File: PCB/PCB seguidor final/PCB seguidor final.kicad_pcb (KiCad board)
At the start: 2 copper layers, 37 parts, among them J2 MOTOR A, J3 MOTOR B, J4 Conn_01x08, J6 Conn_01x04, SW1 SW_SPDT, U2 ESP32-DEVKIT-V1, U3 LM7805, U4 ROB-14450, U5 ROB-14450, U6 module_mpu6050

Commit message: avance
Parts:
- moved J6 209.0 mm to (264.3, 137.1)
- moved U2 202.9 mm to (228.9, 92.0)
- moved J4 186.5 mm to (266.0, 100.0), turned to 180 degrees
- moved U6 183.9 mm to (261.1, 83.3), turned to 60 degrees
- moved U7 142.4 mm to (169.5, 125.9)
- moved U1 128.0 mm to (169.0, 75.2)
- moved U4 112.4 mm to (158.0, 115.5), turned to -90 degrees
- moved U3 99.2 mm to (17.6, 124.3)
- moved U5 77.8 mm to (157.7, 68.0), turned to -90 degrees
- moved C3 67.9 mm to (29.6, 156.1)
- moved .1 54.8 mm to (83.8, 121.1)
- moved C4 37.9 mm to (44.3, 127.5)
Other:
- board outline added: 149.7 x 69.6 mm

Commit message: Acabada(esperando corrección)
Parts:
- moved S2 135.2 mm to (177.9, 127.0)
- moved S1 133.4 mm to (177.9, 115.9)
- moved S4 127.6 mm to (188.0, 122.3)
- moved GND1 127.4 mm to (202.2, 120.9), turned to 90 degrees
- moved R2 122.1 mm to (193.1, 118.3), turned to -90 degrees
- moved S3 118.4 mm to (167.5, 122.2)
- moved R4 117.1 mm to (190.7, 118.2), turned to -90 degrees
- moved C3 108.9 mm to (120.4, 96.1)
- moved R1 107.9 mm to (171.7, 118.1), turned to -90 degrees
- moved R3 103.0 mm to (169.8, 118.1), turned to -90 degrees
- moved U3 96.6 mm to (110.0, 96.2)
- moved TURBINA1 81.0 mm to (161.8, 110.0), turned to 180 degrees
- moved H3 78.4 mm to (97.9, 129.7)
- moved C2 78.2 mm to (98.7, 96.0)
- moved C1 77.7 mm to (98.8, 84.6), turned to 180 degrees
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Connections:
- GND1 pad 3: VCC -> +5V
- SW1 pad 1: unconnected-(SW1-A-Pad1) -> +7.5V
- U2 pad 12: BTN 1 -> BTN 2
- U2 pad 13: BTN 2 -> BTN 4
- U2 pad 17: BTN 4 -> BTN 1
- U2 pad 21: MOTOR B2 -> MOTOR B1
- U2 pad 22: MOTOR B1 -> MOTOR B2
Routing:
- net VCC: track 0.00 -> 189.0 mm
- net VIN M2: track 0.00 -> 155.5 mm
- net +5V: track 0.00 -> 116.9 mm, vias 0 -> 7
- net PWM_B2: track 0.00 -> 107.7 mm, vias 0 -> 1
- net +3.3V: track 0.00 -> 106.6 mm, vias 0 -> 1
- net GND: track 0.00 -> 105.9 mm, vias 0 -> 2
- net PWM_B1: track 0.00 -> 102.7 mm, vias 0 -> 1
- net MOTOR B2: track 0.00 -> 95.2 mm
- net MOTOR B1: track 0.00 -> 94.3 mm
- net PWM_A1: track 0.00 -> 85.1 mm, vias 0 -> 2
- net D: track 0.00 -> 81.1 mm
- net BTN 2: track 0.00 -> 80.4 mm, vias 0 -> 1
- net BTN 4: track 0.00 -> 77.4 mm, vias 0 -> 1
- net BTN 3: track 0.00 -> 73.5 mm, vias 0 -> 1
- net BTN 1: track 0.00 -> 69.0 mm, vias 0 -> 1
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- added copper zone on F.Cu, net +5V
- added copper zone on B.Cu, net GND
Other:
- board size 149.7 x 69.6 mm -> 149.7 x 80 mm

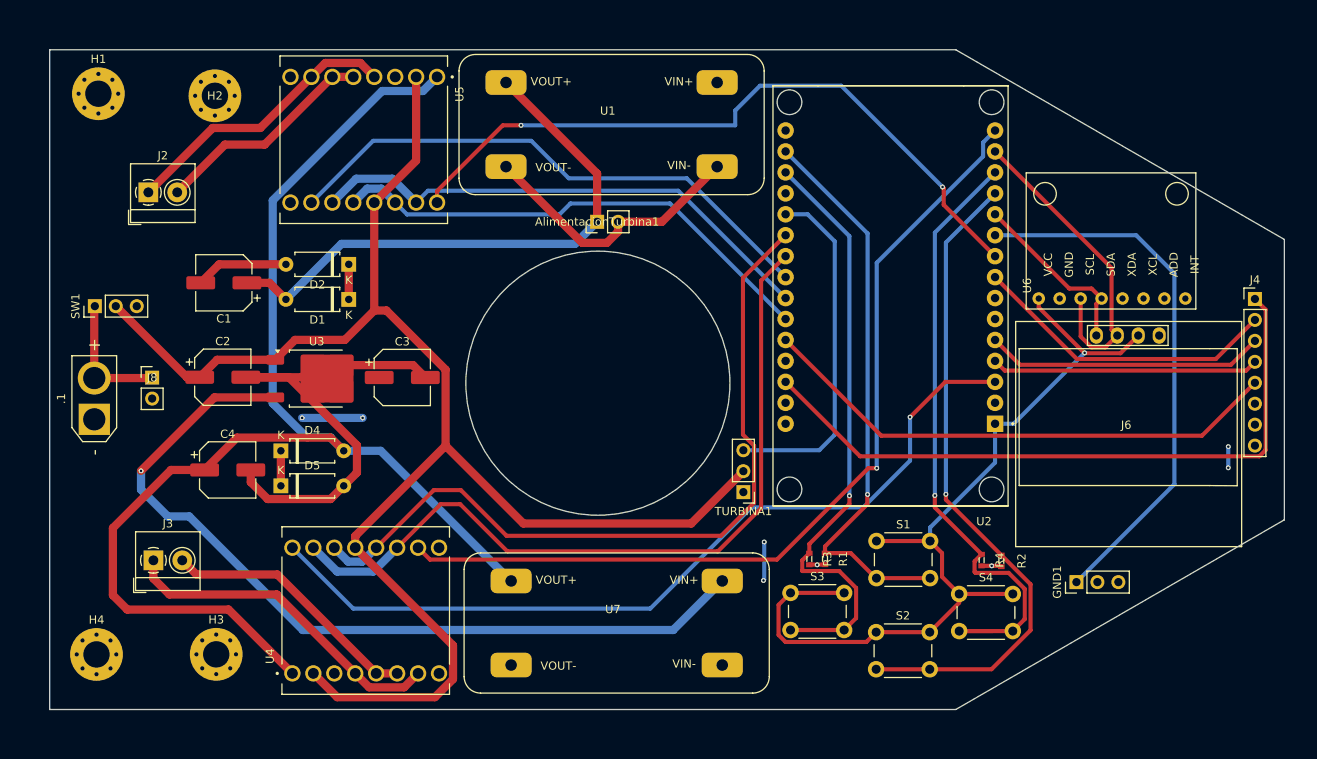
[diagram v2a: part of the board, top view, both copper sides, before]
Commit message: Algunas correcciones hechas
Flata poner led de encendido general y turbina, hacerla un poco mas estetica
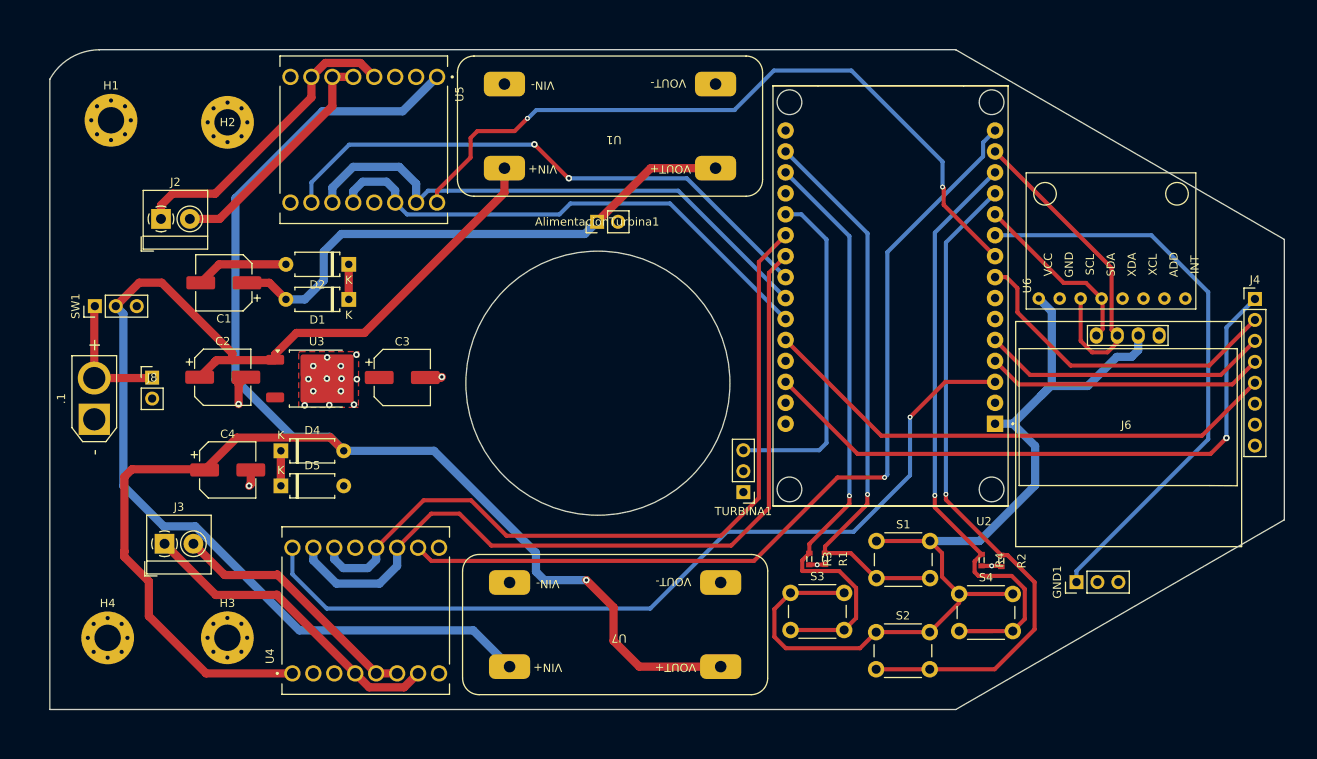
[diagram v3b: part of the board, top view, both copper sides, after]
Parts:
- moved U1 40.5 mm to (164.1, 57.1), turned to 180 degrees
- moved U7 40.5 mm to (164.7, 117.5), turned to 180 degrees
- moved H1 3.57 mm to (85.1, 64.9)
- moved H2 3.57 mm to (99.2, 65.1)
- moved J2 3.57 mm to (91.2, 76.8)
- moved H4 2.42 mm to (84.7, 127.7)
- moved H3 2.42 mm to (99.2, 127.6)
- moved J3 2.42 mm to (91.6, 116.2)
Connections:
- TURBINA1 pad 2: VCC -> +5V
- U1 pad 2: +5V -> VCC
- U4 pad 13: VCC -> +5V
- U4 pad 2: VCC -> +5V
- U5 pad 13: VCC -> +5V
- U5 pad 2: VCC -> +5V
- U7 pad 2: +5V -> VCC
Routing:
- net +5V: track 116.9 -> 0.00 mm, vias 7 -> 0
- net GND: track 105.9 -> 23.3 mm, vias 2 -> 18
- net VIN M2: track 155.5 -> 197.2 mm, vias 0 -> 1
- net VCC: track 189.0 -> 147.4 mm
- net +3.3V: track 106.6 -> 119.7 mm, vias 1 -> 0
- net D: track 81.1 -> 76.2 mm, vias 0 -> 1
- net SIGNAL: track 66.0 -> 70.5 mm
- net PWM_A1: track 85.1 -> 88.8 mm
- net MOTOR A2: track 63.3 -> 66.9 mm
- net PWM_B1: track 102.7 -> 105.7 mm
- net MOTOR B2: track 95.2 -> 97.6 mm
- net MOTOR A1: track 60.8 -> 63.1 mm
- net C: track 37.6 -> 40.0 mm
- net VIN M: track 68.7 -> 66.3 mm
- net OUT A1: track 34.6 -> 36.8 mm
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- added copper zone on F.Cu, net GND
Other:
- outline, holes or cut-outs redrawn

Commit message: Correcciones hechas
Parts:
- added D3: LED, LED_SMD:LED_miniPLCC_2315_Handsoldering, F.Cu at (83.2, 79.4)
- added D6: LED, LED_SMD:LED_miniPLCC_2315_Handsoldering, F.Cu at (134.1, 76.2)
- added R5: 10K, digikey-kicad-library-master:0603, F.Cu at (83.0, 82.5)
- added R6: 10K, digikey-kicad-library-master:0603, F.Cu at (132.4, 79.8)
- added SW2: SW_SPDT, Connector_PinHeader_2.54mm:PinHeader_1x03_P2.54mm_Vertical, F.Cu at (126.5, 86.1)
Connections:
- U1 pad 2: VCC -> Ve
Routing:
- net Ve: track 0.00 -> 21.8 mm
- net VCC: track 147.4 -> 132.9 mm
- net GND: track 23.3 -> 29.9 mm, vias 18 -> 20
- net Net-(D6-A): track 0.00 -> 3.59 mm
- net Net-(D3-A): track 0.00 -> 3.17 mm
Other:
- outline, holes or cut-outs redrawn
